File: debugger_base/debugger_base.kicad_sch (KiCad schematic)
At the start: 38 parts, among them SW1 RST_FT, X1 USB_C_Receptacle_USB2.0_14P, X2 Conn_02x18_Top_Bottom, Y1 12MHz

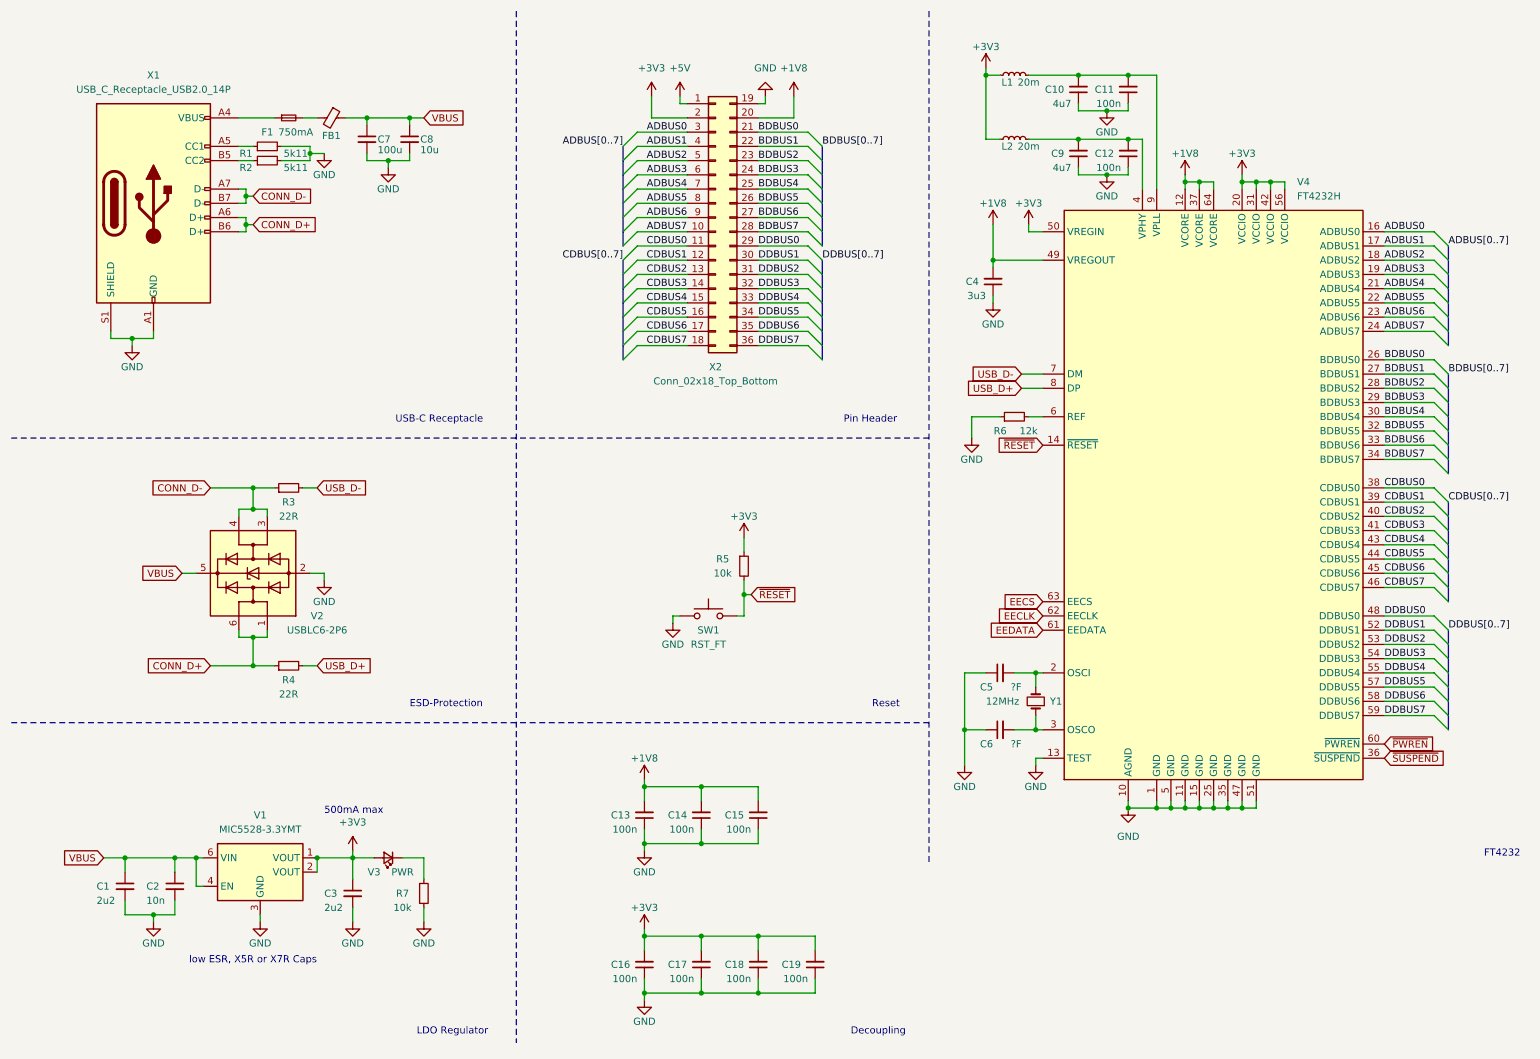
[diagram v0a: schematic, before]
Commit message: add rx/tx status leds
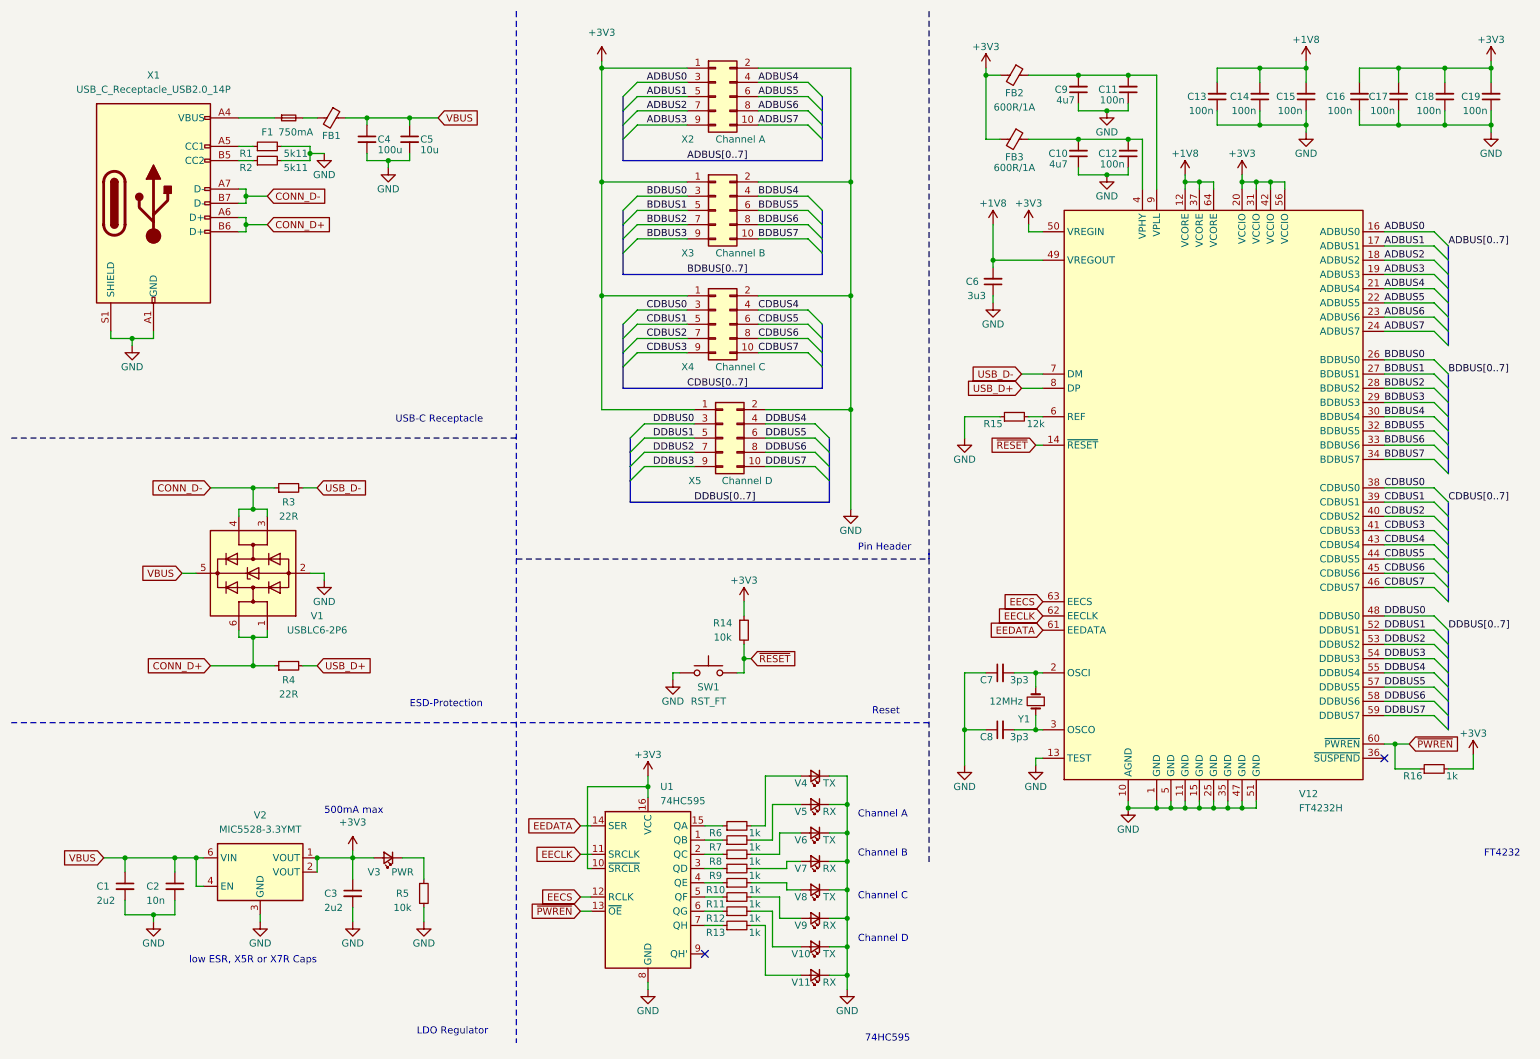
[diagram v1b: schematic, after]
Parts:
- removed L1, L2: 20m, symbol Device:L_Small
- removed X2: Conn_02x18_Top_Bottom, Connector_PinHeader_1.27mm:PinHeader_2x18_P1.27mm_Vertical, symbol Connector_Generic:Conn_02x18_Top_Bottom
- added FB2, FB3: 600R/1A, Inductor_SMD:L_0603_1608Metric, symbol Device:FerriteBead_Small
- added R10, R11, R12, R13, R16, R6, R7, R8, R9: 1k, Resistor_SMD:R_0402_1005Metric_Pad0.72x0.64mm_HandSolder, symbol Device:R_Small
- added U1: 74HC595, symbol 74xx:74HC595
- added V10, V4, V6, V8: TX, LED_SMD:LED_0603_1608Metric, symbol Device:LED_Small
- added V11, V5, V7, V9: RX, LED_SMD:LED_0603_1608Metric, symbol Device:LED_Small
- added X2: Channel A, Connector_PinHeader_2.54mm:PinHeader_2x05_P2.54mm_Vertical_SMD, symbol Connector_Generic:Conn_02x05_Odd_Even
- added X3: Channel B, Connector_PinHeader_2.54mm:PinHeader_2x05_P2.54mm_Vertical_SMD, symbol Connector_Generic:Conn_02x05_Odd_Even
- added X4: Channel C, Connector_PinHeader_2.54mm:PinHeader_2x05_P2.54mm_Vertical_SMD, symbol Connector_Generic:Conn_02x05_Odd_Even
- added X5: Channel D, Connector_PinHeader_2.54mm:PinHeader_2x05_P2.54mm_Vertical_SMD, symbol Connector_Generic:Conn_02x05_Odd_Even
- C7: renamed from C5; value ?F -> 3p3
- C8: renamed from C6; value ?F -> 3p3
- SW1: footprint (none) -> myLib:SW_SPST_EVQP2
- V3: footprint (none) -> LED_SMD:LED_0603_1608Metric
- Y1: footprint (none) -> Crystal:Crystal_SMD_3225-4Pin_3.2x2.5mm
- renumbered C9 to C10, C7 to C4, C8 to C5, C4 to C6, C10 to C9, R5 to R14, R6 to R15, R7 to R5, V2 to V1, V4 to V12, V1 to V2
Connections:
- net +3V3: now also FB2.2, FB3.2, R16.2, U1.10 (~{SRCLR}), U1.16 (VCC), X2.1 (Pin_1), X3.1 (Pin_1), X4.1 (Pin_1), X5.1 (Pin_1)
- net ADBUS0: now also X2.3 (Pin_3)
- net ADBUS1: now also X2.5 (Pin_5)
- net ADBUS2: now also X2.7 (Pin_7)
- net ADBUS3: now also X2.9 (Pin_9)
- net ADBUS4: now also X2.4 (Pin_4)
- net ADBUS5: now also X2.6 (Pin_6)
- net ADBUS6: now also X2.8 (Pin_8)
- net ADBUS7: now also X2.10 (Pin_10)
- net BDBUS0: now also X3.3 (Pin_3)
- net BDBUS1: now also X3.5 (Pin_5)
- net BDBUS2: now also X3.7 (Pin_7)
- net BDBUS3: now also X3.9 (Pin_9)
- net BDBUS4: now also X3.4 (Pin_4)
- net BDBUS5: now also X3.6 (Pin_6)
- net BDBUS6: now also X3.8 (Pin_8)
- net BDBUS7: now also X3.10 (Pin_10)
- net CDBUS0: now also X4.3 (Pin_3)
- net CDBUS1: now also X4.5 (Pin_5)
- net CDBUS2: now also X4.7 (Pin_7)
- net CDBUS3: now also X4.9 (Pin_9)
- net CDBUS4: now also X4.4 (Pin_4)
- net CDBUS5: now also X4.6 (Pin_6)
- net CDBUS6: now also X4.8 (Pin_8)
- net CDBUS7: now also X4.10 (Pin_10)
- net DDBUS0: now also X5.3 (Pin_3)
- net DDBUS1: now also X5.5 (Pin_5)
- net DDBUS2: now also X5.7 (Pin_7)
- net DDBUS3: now also X5.9 (Pin_9)
- net DDBUS4: now also X5.4 (Pin_4)
- net DDBUS5: now also X5.6 (Pin_6)
- net DDBUS6: now also X5.8 (Pin_8)
- net DDBUS7: now also X5.10 (Pin_10)
- net EECLK: now also U1.11 (SRCLK)
- net EECS: now also U1.12 (RCLK)
- net EEDATA: now also U1.14 (SER)
- net ~{PWREN}: now also R16.1, U1.13 (~{OE})
- net at C11.2, C9.2, V12.9 (VPLL): now also FB2.1
- net at C10.2, C12.2, V12.4 (VPHY): now also FB3.1
- net EP renamed GND
- net GND: now also U1.8 (GND), V10.1 (K), V11.1 (K), V4.1 (K), V5.1 (K), V6.1 (K), V7.1 (K), V8.1 (K), V9.1 (K), X2.2 (Pin_2), X3.2 (Pin_2), X4.2 (Pin_2), X5.2 (Pin_2)
- net ~{SUSPEND}: no longer names the net of V12.36 (~{SUSPEND})
- new net: R8.1, U1.2 (QC)
- new net: R8.2, V6.2 (A)
- new net: R7.1, U1.1 (QB)
- new net: R6.1, U1.15 (QA)
- new net: R9.1, U1.3 (QD)
- new net: R10.1, U1.4 (QE)
- new net: R11.1, U1.5 (QF)
- new net: R12.1, U1.6 (QG)
- new net: R13.1, U1.7 (QH)
- new net: R9.2, V7.2 (A)
- new net: R12.2, V10.2 (A)
- new net: R13.2, V11.2 (A)
- new net: R11.2, V9.2 (A)
- new net: R10.2, V8.2 (A)
- new net: R7.2, V5.2 (A)
- new net: R6.2, V4.2 (A)
- no-connect marks 0 -> 2
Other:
- note added: "74HC595"
- note added: "Channel A"
- note added: "Channel B"
- note added: "Channel C"
- note added: "Channel D"
- note removed: "Decoupling"
- moved on the sheet: C13, C14, C15, C16, C17, C18, C19, R14, SW1

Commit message: exclude traffic leds from base board
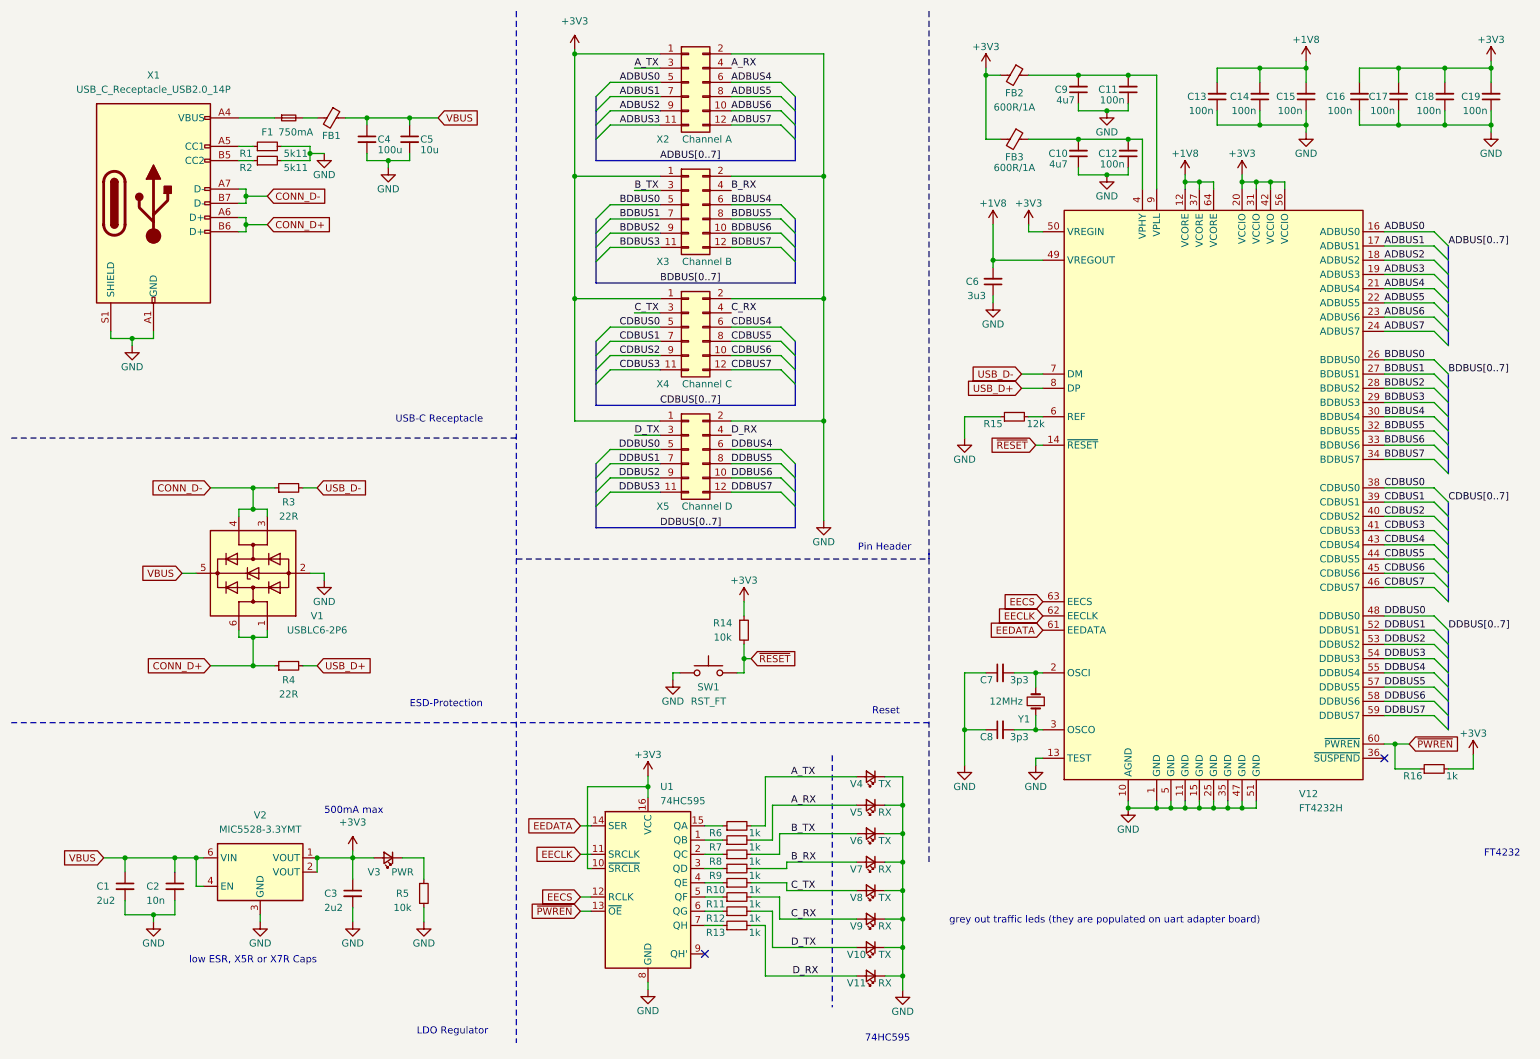
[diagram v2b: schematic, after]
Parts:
- removed X2: Channel A, Connector_PinHeader_2.54mm:PinHeader_2x05_P2.54mm_Vertical_SMD, symbol Connector_Generic:Conn_02x05_Odd_Even
- removed X3: Channel B, Connector_PinHeader_2.54mm:PinHeader_2x05_P2.54mm_Vertical_SMD, symbol Connector_Generic:Conn_02x05_Odd_Even
- removed X4: Channel C, Connector_PinHeader_2.54mm:PinHeader_2x05_P2.54mm_Vertical_SMD, symbol Connector_Generic:Conn_02x05_Odd_Even
- removed X5: Channel D, Connector_PinHeader_2.54mm:PinHeader_2x05_P2.54mm_Vertical_SMD, symbol Connector_Generic:Conn_02x05_Odd_Even
- added X2: Channel A, Connector_PinHeader_2.54mm:PinHeader_2x06_P2.54mm_Vertical_SMD, symbol Connector_Generic:Conn_02x06_Odd_Even
- added X3: Channel B, Connector_PinHeader_2.54mm:PinHeader_2x06_P2.54mm_Vertical_SMD, symbol Connector_Generic:Conn_02x06_Odd_Even
- added X4: Channel C, Connector_PinHeader_2.54mm:PinHeader_2x06_P2.54mm_Vertical_SMD, symbol Connector_Generic:Conn_02x06_Odd_Even
- added X5: Channel D, Connector_PinHeader_2.54mm:PinHeader_2x06_P2.54mm_Vertical_SMD, symbol Connector_Generic:Conn_02x06_Odd_Even
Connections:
- net +3V3: now also X2.1 (Pin_1), X3.1 (Pin_1), X4.1 (Pin_1), X5.1 (Pin_1)
- net ADBUS0: now also X2.5 (Pin_5)
- net ADBUS1: now also X2.7 (Pin_7)
- net ADBUS2: now also X2.9 (Pin_9)
- net ADBUS3: now also X2.11 (Pin_11)
- net ADBUS4: now also X2.6 (Pin_6)
- net ADBUS5: now also X2.8 (Pin_8)
- net ADBUS6: now also X2.10 (Pin_10)
- net ADBUS7: now also X2.12 (Pin_12)
- net BDBUS0: now also X3.5 (Pin_5)
- net BDBUS1: now also X3.7 (Pin_7)
- net BDBUS2: now also X3.9 (Pin_9)
- net BDBUS3: now also X3.11 (Pin_11)
- net BDBUS4: now also X3.6 (Pin_6)
- net BDBUS5: now also X3.8 (Pin_8)
- net BDBUS6: now also X3.10 (Pin_10)
- net BDBUS7: now also X3.12 (Pin_12)
- net CDBUS0: now also X4.5 (Pin_5)
- net CDBUS1: now also X4.7 (Pin_7)
- net CDBUS2: now also X4.9 (Pin_9)
- net CDBUS3: now also X4.11 (Pin_11)
- net CDBUS4: now also X4.6 (Pin_6)
- net CDBUS5: now also X4.8 (Pin_8)
- net CDBUS6: now also X4.10 (Pin_10)
- net CDBUS7: now also X4.12 (Pin_12)
- net DDBUS0: now also X5.5 (Pin_5)
- net DDBUS1: now also X5.7 (Pin_7)
- net DDBUS2: now also X5.9 (Pin_9)
- net DDBUS3: now also X5.11 (Pin_11)
- net DDBUS4: now also X5.6 (Pin_6)
- net DDBUS5: now also X5.8 (Pin_8)
- net DDBUS6: now also X5.10 (Pin_10)
- net DDBUS7: now also X5.12 (Pin_12)
- net GND: now also X2.2 (Pin_2), X3.2 (Pin_2), X4.2 (Pin_2), X5.2 (Pin_2)
- net B_TX: now reaches R8.2, V6.2 (A)
- net B_TX: now also X3.3 (Pin_3)
- net B_RX: now reaches R9.2, V7.2 (A)
- net B_RX: now also X3.4 (Pin_4)
- net D_TX: now reaches R12.2, V10.2 (A)
- net D_TX: now also X5.3 (Pin_3)
- net D_RX: now reaches R13.2, V11.2 (A)
- net D_RX: now also X5.4 (Pin_4)
- net C_RX: now reaches R11.2, V9.2 (A)
- net C_RX: now also X4.4 (Pin_4)
- net C_TX: now reaches R10.2, V8.2 (A)
- net C_TX: now also X4.3 (Pin_3)
- net A_RX: now reaches R7.2, V5.2 (A)
- net A_RX: now also X2.4 (Pin_4)
- net A_TX: now reaches R6.2, V4.2 (A)
- net A_TX: now also X2.3 (Pin_3)
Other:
- note added: "grey out traffic leds (they are populated on uart adapter board)"
- note removed: "Channel A"
- note removed: "Channel B"
- note removed: "Channel C"
- note removed: "Channel D"
- moved on the sheet: V10, V11, V4, V5, V6, V7, V8, V9
